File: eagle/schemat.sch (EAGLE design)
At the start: 30 parts, among them IC1 MEGA8-AI, Q1 N-MOSFET BSS138, Q2 N-MOSFET BSS138, U1 LCD-16X2SILK, Y1 16MHz

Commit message: Gotowa płytka
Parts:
- removed D1: GREEN, SparkFun-LED:LED-GREEN0603
- removed D2: RED, SparkFun-LED:LED-RED0603
- removed JP1, JP2, JP6, JP7: M02PTH, SparkFun-Connectors:M02PTH
- removed R3, R4: 100, SparkFun-Passives:RESISTOR0805-RES
- added PRZYCISKI_+-, PRZYCISKI_MIESZ_TEMP: (no value), SparkFun-Connectors:M03LOCK
- added TEMP_PRZEKAZNIK1, TEMP_PRZEKAZNIK2: M01PTH, SparkFun-Connectors:M01PTH
- added X2: MINI-USB-32005-301, con-cypressindustries:MINI-USB-32005-301
- L1: device inductors:MICC10 -> SparkFun-Passives:INDUCTOR0805
- renumbered JP10 to MIESZANIE_PRZEKAZNIK, JP3 to TEMP, JP4 to MIESZANIE, JP5 to ZAPISZ, JP8 to NAPIECIE, JP9 to TEMP_PRZEKAZNIK
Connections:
- removed net N$10: D2.C, R4.2
- removed net N$11: D1.A, IC1.PD0(RXD)
- removed net N$12: D1.C, R3.2
- removed net N$8: D2.A, IC1.PD1(TXD)
- new net MISO: IC1.PB4(MISO), X2.3
- new net MOSI: IC1.PB3(MOSI/OC2), X2.2
- new net SCK: IC1.PB5(SCK), X2.4
- net +5V: now also NAPIECIE.1, U$1.C, X2.1
- net DB4: now also IC1.PD7(AIN1); no longer IC1.PB2(SS/OC1B)
- net DB5: now also IC1.PB0(ICP); no longer IC1.PB3(MOSI/OC2)
- net DB6: now also IC1.PB1(OC1A); no longer IC1.PB4(MISO)
- net DB7: now also IC1.PB2(SS/OC1B); no longer IC1.PB5(SCK)
- net E: now also IC1.PD6(AIN0); no longer IC1.PB1(OC1A)
- net GND: now also PRZYCISKI_+-.3, PRZYCISKI_MIESZ_TEMP.3, X2.5; no longer JP1.2, JP2.2, JP6.2, JP7.2, R3.1, R4.1
- net MIESZANIE: now also IC1.PC5(ADC5/SCL); no longer IC1.PC4(ADC4/SDA)
- net PRZYCISK+: now also PRZYCISKI_+-.2; no longer JP6.1
- net PRZYCISK-: now also PRZYCISKI_+-.1; no longer JP7.1
- net PRZYCISK_MIESZANIE: now also IC1.PC4(ADC4/SDA), PRZYCISKI_MIESZ_TEMP.1; no longer IC1.PC2(ADC2), JP2.1
- net PRZYCISK_TEMP: now also IC1.PC3(ADC3), PRZYCISKI_MIESZ_TEMP.2; no longer IC1.PC1(ADC1), JP1.1
- net RS: now also IC1.PD5(T1); no longer IC1.PB0(ICP)
- net TEMP: now also IC1.PC2(ADC2); no longer IC1.PC3(ADC3)
- net VCC: no longer NAPIECIE.1, U$1.C
- net VDD: now also TEMP_PRZEKAZNIK1.1, TEMP_PRZEKAZNIK2.1
- net ZAPISZ: now also IC1.PC1(ADC1); no longer IC1.PC5(ADC5/SCL)

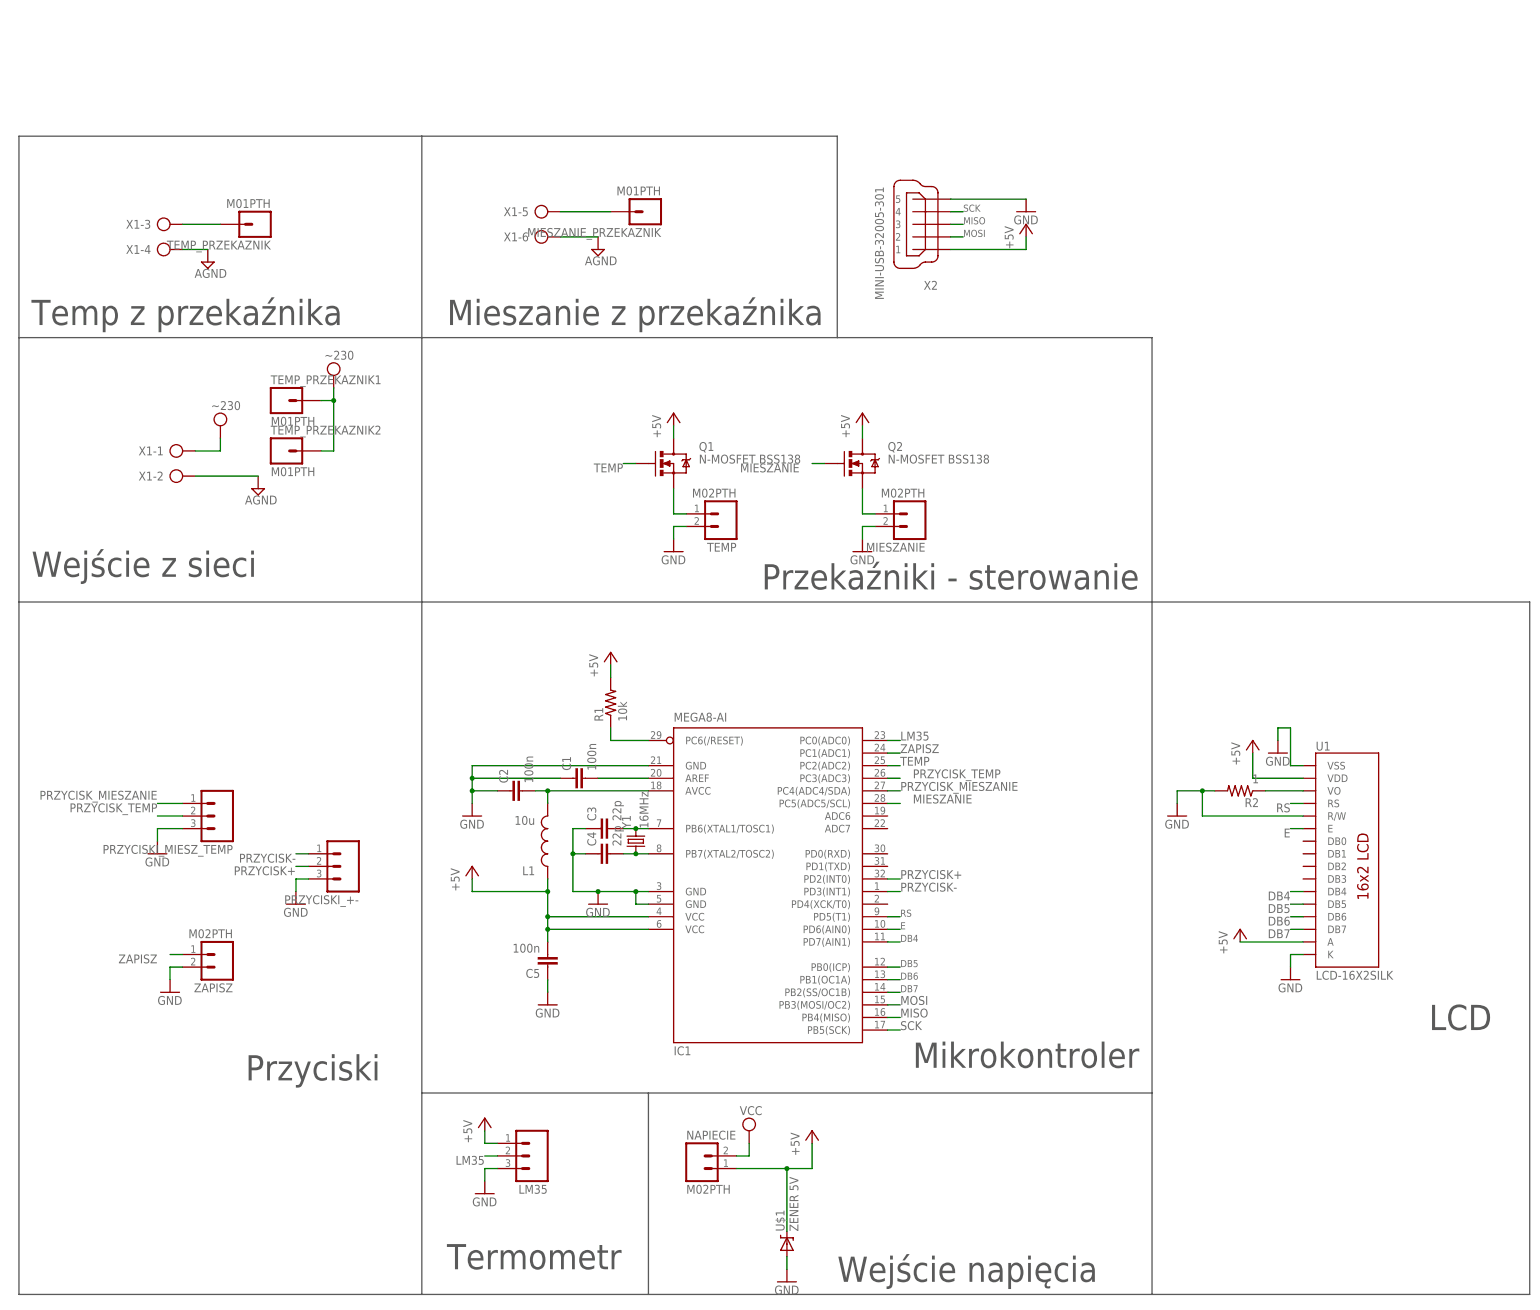
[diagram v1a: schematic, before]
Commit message: Poprawiony schemat
Nie dało się przylutować microUSB (zła biblioteka)
Nie podłączony RESET
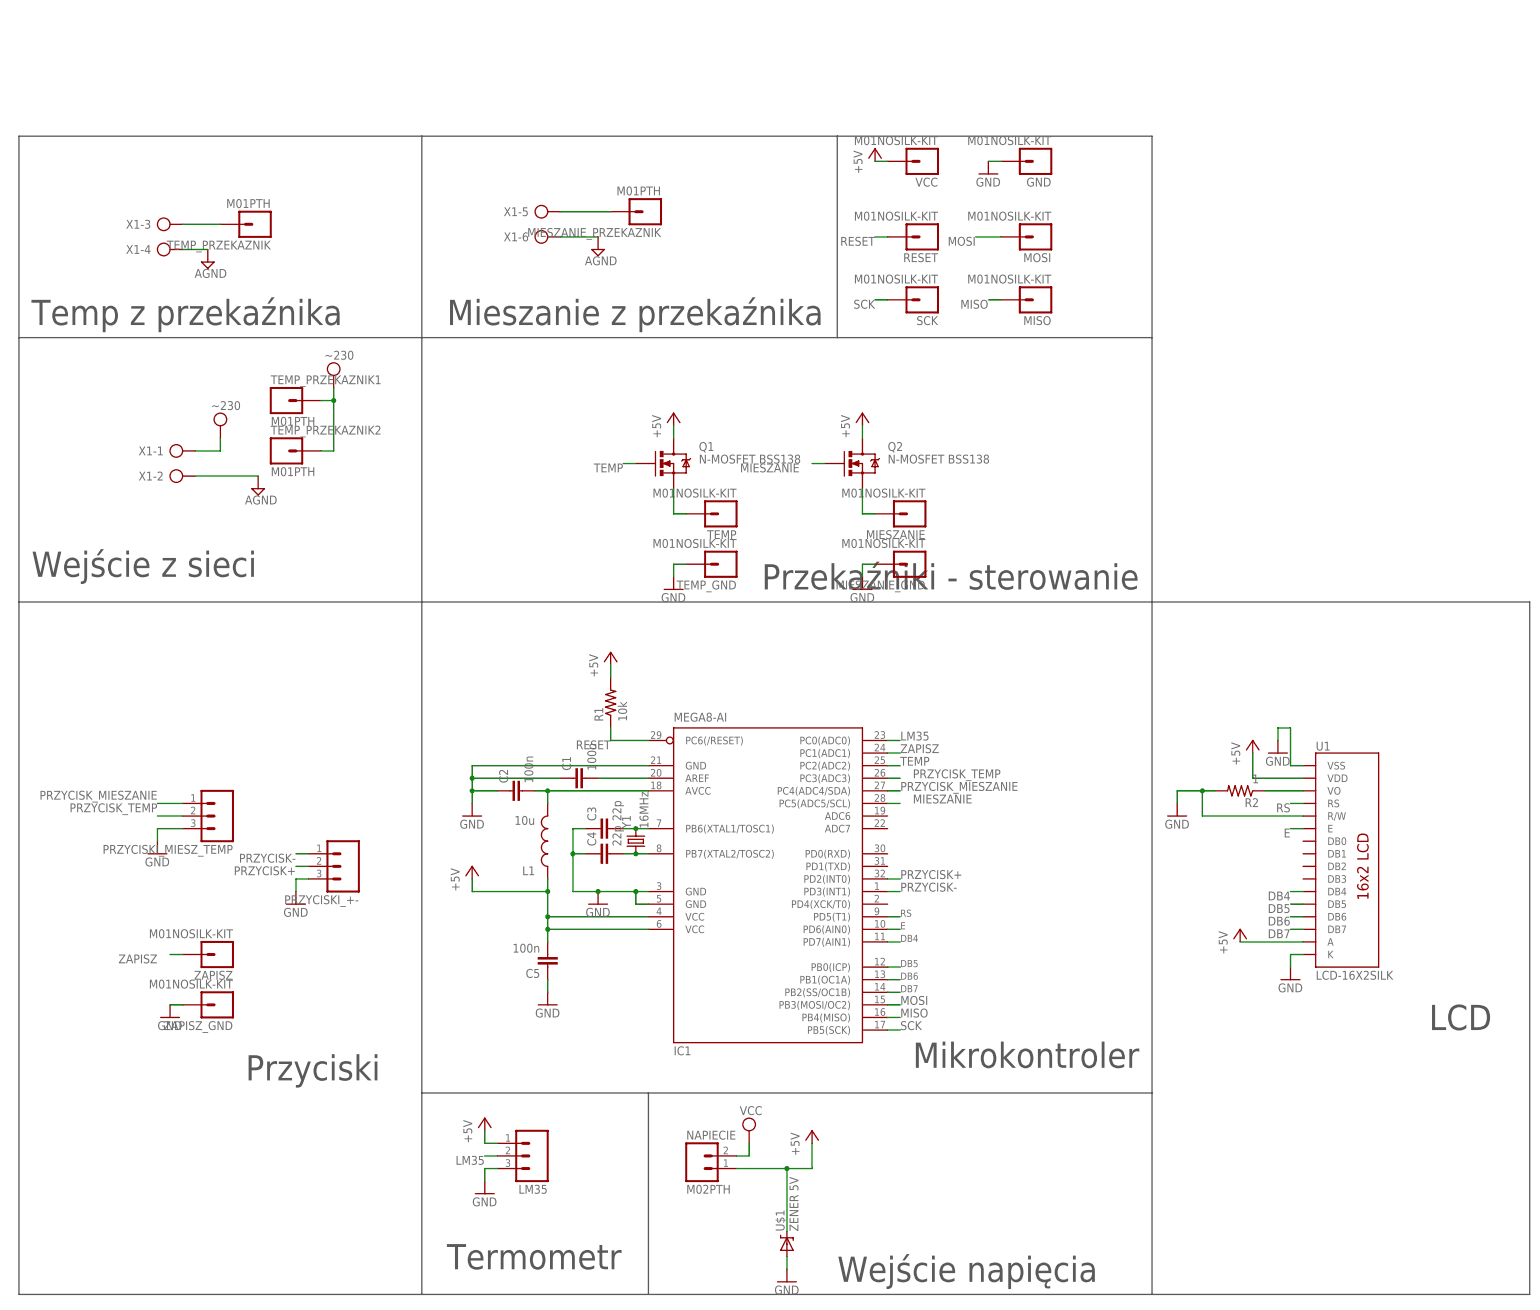
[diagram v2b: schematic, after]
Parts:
- removed X2: MINI-USB-32005-301, con-cypressindustries:MINI-USB-32005-301
- added GND, MIESZANIE_GND, MISO, MOSI, RESET, SCK, TEMP_GND, VCC, ZAPISZ_GND: M01NOSILK-KIT, SparkFun-Connectors:M01NOSILK-KIT
- MIESZANIE, TEMP, ZAPISZ: value M02PTH -> M01NOSILK-KIT; device SparkFun-Connectors:M02PTH -> SparkFun-Connectors:M01NOSILK-KIT
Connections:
- removed net N$1: IC1.PC6(/RESET), R1.1
- new net RESET: IC1.PC6(/RESET), R1.1, RESET.1
- net +5V: now also VCC.1; no longer X2.1
- net GND: now also GND.1, MIESZANIE_GND.1, TEMP_GND.1, ZAPISZ_GND.1; no longer MIESZANIE.2, TEMP.2, X2.5, ZAPISZ.2
- net MISO: now also MISO.1; no longer X2.3
- net MOSI: now also MOSI.1; no longer X2.2
- net SCK: now also SCK.1; no longer X2.4
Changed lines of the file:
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@@
 <part name="P+4" library="supply1" deviceset="+5V" device=""/>
 <part name="P+5" library="supply1" deviceset="+5V" device=""/>
-<part name="TEMP" library="SparkFun-Connectors" deviceset="M02" device="PTH"/>
-<part name="MIESZANIE" library="SparkFun-Connectors" deviceset="M02" device="PTH"/>
-<part name="GND7" library="SparkFun-Aesthetics" deviceset="GND" device=""/>
-<part name="GND8" library="SparkFun-Aesthetics" deviceset="GND" device=""/>
-<part name="ZAPISZ" library="SparkFun-Connectors" deviceset="M02" device="PTH"/>
-<part name="GND9" library="SparkFun-Aesthetics" deviceset="GND" device=""/>
+<part name="TEMP" library="SparkFun-Connectors" deviceset="M01" device="NOSILK-KIT"/>
+<part name="MIESZANIE" library="SparkFun-Connectors" deviceset="M01" device="NOSILK-KIT"/>
+<part name="ZAPISZ" library="SparkFun-Connectors" deviceset="M01" device="NOSILK-KIT" value="M01NOSILK-KIT"/>
 <part name="U1" library="SparkFun-Displays" deviceset="LCD-16X2" device="SILK"/>
 <part name="GND10" library="SparkFun-Aesthetics" deviceset="GND" device=""/>
@@
 <part name="TEMP_PRZEKAZNIK2" library="SparkFun-Connectors" deviceset="M01" device="PTH"/>
 <part name="SUPPLY6" library="supply2" deviceset="VDD" device="" value="~230"/>
-<part name="X2" library="con-cypressindustries" deviceset="MINI-USB-" device="32005-301"/>
+<part name="ZAPISZ_GND" library="SparkFun-Connectors" deviceset="M01" device="NOSILK-KIT"/>
+<part name="GND9" library="SparkFun-Aesthetics" deviceset="GND" device=""/>
+<part name="VCC" library="SparkFun-Connectors" deviceset="M01" device="NOSILK-KIT"/>
+<part name="GND" library="SparkFun-Connectors" deviceset="M01" device="NOSILK-KIT"/>
+<part name="RESET" library="SparkFun-Connectors" deviceset="M01" device="NOSILK-KIT"/>
+<part name="MOSI" library="SparkFun-Connectors" deviceset="M01" device="NOSILK-KIT"/>
+<part name="SCK" library="SparkFun-Connectors" deviceset="M01" device="NOSILK-KIT"/>
+<part name="MISO" library="SparkFun-Connectors" deviceset="M01" device="NOSILK-KIT"/>
 <part name="P+9" library="supply1" deviceset="+5V" device=""/>
 <part name="GND6" library="SparkFun-Aesthetics" deviceset="GND" device=""/>
+<part name="TEMP_GND" library="SparkFun-Connectors" deviceset="M01" device="NOSILK-KIT"/>
+<part name="MIESZANIE_GND" library="SparkFun-Connectors" deviceset="M01" device="NOSILK-KIT"/>
+<part name="GND7" library="SparkFun-Aesthetics" deviceset="GND" device=""/>
+<part name="GND8" library="SparkFun-Aesthetics" deviceset="GND" device=""/>
 </parts>
 <sheets>
@@
 <wire x1="63.5" y1="208.28" x2="63.5" y2="167.64" width="0.1524" layer="97"/>
 <text x="-15.24" y="170.18" size="5.08" layer="97">Mieszanie z przekaźnika</text>
+<wire x1="127" y1="167.64" x2="127" y2="208.28" width="0.1524" layer="97"/>
+<wire x1="127" y1="208.28" x2="63.5" y2="208.28" width="0.1524" layer="97"/>
 </plain>
 <instances>
@@
 <instance part="TEMP" gate="G$1" x="40.64" y="132.08" rot="R180"/>
 <instance part="MIESZANIE" gate="G$1" x="78.74" y="132.08" rot="R180"/>
-<instance part="GND7" gate="1" x="30.48" y="124.46"/>
-<instance part="GND8" gate="1" x="68.58" y="124.46"/>
 <instance part="ZAPISZ" gate="G$1" x="-60.96" y="43.18" rot="R180"/>
-<instance part="GND9" gate="1" x="-71.12" y="35.56"/>
 <instance part="U1" gate="G$1" x="167.64" y="60.96"/>
 <instance part="GND10" gate="1" x="154.94" y="38.1"/>
@@
 <instance part="TEMP_PRZEKAZNIK2" gate="G$1" x="-48.26" y="144.78"/>
 <instance part="SUPPLY6" gate="G$1" x="-38.1" y="160.02"/>
-<instance part="X2" gate="G$1" x="81.28" y="190.5" rot="R180"/>
-<instance part="P+9" gate="1" x="101.6" y="190.5"/>
-<instance part="GND6" gate="1" x="101.6" y="193.04"/>
+<instance part="ZAPISZ_GND" gate="G$1" x="-60.96" y="33.02" rot="R180"/>
+<instance part="GND9" gate="1" x="-71.12" y="30.48"/>
+<instance part="VCC" gate="G$1" x="81.28" y="203.2" rot="R180"/>
+<instance part="GND" gate="G$1" x="104.14" y="203.2" rot="R180"/>
+<instance part="RESET" gate="G$1" x="81.28" y="187.96" rot="R180"/>
+<instance part="MOSI" gate="G$1" x="104.14" y="187.96" rot="R180"/>
+<instance part="SCK" gate="G$1" x="81.28" y="175.26" rot="R180"/>
+<instance part="MISO" gate="G$1" x="104.14" y="175.26" rot="R180"/>
+<instance part="P+9" gate="1" x="71.12" y="205.74"/>
+<instance part="GND6" gate="1" x="93.98" y="200.66"/>
+<instance part="TEMP_GND" gate="G$1" x="40.64" y="121.92" rot="R180"/>
+<instance part="MIESZANIE_GND" gate="G$1" x="78.74" y="121.92" rot="R180"/>
+<instance part="GND7" gate="1" x="30.48" y="116.84"/>
+<instance part="GND8" gate="1" x="68.58" y="116.84"/>
 </instances>
 <busses>
@@
 </segment>
 <segment>
-<pinref part="X2" gate="G$1" pin="1"/>
-<wire x1="86.36" y1="185.42" x2="101.6" y2="185.42" width="0.1524" layer="91"/>
-<wire x1="101.6" y1="185.42" x2="101.6" y2="187.96" width="0.1524" layer="91"/>
+<pinref part="VCC" gate="G$1" pin="1"/>
+<wire x1="73.66" y1="203.2" x2="71.12" y2="203.2" width="0.1524" layer="91"/>
 <pinref part="P+9" gate="1" pin="+5V"/>
 </segment>
 </net>
-<net name="N$1" class="0">
+<net name="RESET" class="0">
 <segment>
 <pinref part="R1" gate="G$1" pin="1"/>
@@
 <pinref part="IC1" gate="G$1" pin="PC6(/RESET)"/>
 <wire x1="17.78" y1="86.36" x2="25.4" y2="86.36" width="0.1524" layer="91"/>
+<label x="17.78" y="86.36" size="1.778" layer="95" rot="R180"/>
+</segment>
+<segment>
+<pinref part="RESET" gate="G$1" pin="1"/>
+<wire x1="73.66" y1="187.96" x2="71.12" y2="187.96" width="0.1524" layer="91"/>
+<label x="71.12" y="187.96" size="1.778" layer="95" rot="R180"/>
 </segment>
 </net>
@@
 </segment>
 <segment>
-<pinref part="MIESZANIE" gate="G$1" pin="2"/>
-<pinref part="GND8" gate="1" pin="GND"/>
-<wire x1="71.12" y1="129.54" x2="68.58" y2="129.54" width="0.1524" layer="91"/>
-<wire x1="68.58" y1="129.54" x2="68.58" y2="127" width="0.1524" layer="91"/>
-</segment>
-<segment>
-<pinref part="TEMP" gate="G$1" pin="2"/>
-<pinref part="GND7" gate="1" pin="GND"/>
-<wire x1="33.02" y1="129.54" x2="30.48" y2="129.54" width="0.1524" layer="91"/>
-<wire x1="30.48" y1="129.54" x2="30.48" y2="127" width="0.1524" layer="91"/>
-</segment>
-<segment>
-<pinref part="ZAPISZ" gate="G$1" pin="2"/>
-<pinref part="GND9" gate="1" pin="GND"/>
-<wire x1="-68.58" y1="40.64" x2="-71.12" y2="40.64" width="0.1524" layer="91"/>
-<wire x1="-71.12" y1="40.64" x2="-71.12" y2="38.1" width="0.1524" layer="91"/>
-</segment>
-<segment>
 <pinref part="U1" gate="G$1" pin="K"/>
 <pinref part="GND10" gate="1" pin="GND"/>
@@
 </segment>
 <segment>
-<pinref part="X2" gate="G$1" pin="5"/>
-<wire x1="86.36" y1="195.58" x2="101.6" y2="195.58" width="0.1524" layer="91"/>
+<pinref part="ZAPISZ_GND" gate="G$1" pin="1"/>
+<wire x1="-68.58" y1="33.02" x2="-71.12" y2="33.02" width="0.1524" layer="91"/>
+<pinref part="GND9" gate="1" pin="GND"/>
+</segment>
+<segment>
+<pinref part="GND" gate="G$1" pin="1"/>
+<wire x1="96.52" y1="203.2" x2="93.98" y2="203.2" width="0.1524" layer="91"/>
 <pinref part="GND6" gate="1" pin="GND"/>
+</segment>
+<segment>
+<pinref part="GND7" gate="1" pin="GND"/>
+<wire x1="30.48" y1="119.38" x2="30.48" y2="121.92" width="0.1524" layer="91"/>
+<pinref part="TEMP_GND" gate="G$1" pin="1"/>
+<wire x1="30.48" y1="121.92" x2="33.02" y2="121.92" width="0.1524" layer="91"/>
+</segment>
+<segment>
+<pinref part="GND8" gate="1" pin="GND"/>
+<wire x1="68.58" y1="119.38" x2="68.58" y2="121.92" width="0.1524" layer="91"/>
+<pinref part="MIESZANIE_GND" gate="G$1" pin="1"/>
+<wire x1="68.58" y1="121.92" x2="71.12" y2="121.92" width="0.1524" layer="91"/>
 </segment>
 </net>
@@
 </segment>
 <segment>
-<pinref part="X2" gate="G$1" pin="2"/>
-<wire x1="86.36" y1="187.96" x2="88.9" y2="187.96" width="0.1524" layer="91"/>
-<label x="88.9" y="187.96" size="1.4224" layer="95"/>
+<pinref part="MOSI" gate="G$1" pin="1"/>
+<wire x1="96.52" y1="187.96" x2="91.44" y2="187.96" width="0.1524" layer="91"/>
+<label x="91.44" y="187.96" size="1.778" layer="95" rot="R180"/>
 </segment>
 </net>
@@
 </segment>
 <segment>
-<pinref part="X2" gate="G$1" pin="3"/>
-<wire x1="86.36" y1="190.5" x2="88.9" y2="190.5" width="0.1524" layer="91"/>
-<label x="88.9" y="190.5" size="1.4224" layer="95"/>
+<pinref part="MISO" gate="G$1" pin="1"/>
+<wire x1="96.52" y1="175.26" x2="93.98" y2="175.26" width="0.1524" layer="91"/>
+<label x="93.98" y="175.26" size="1.778" layer="95" rot="R180"/>
 </segment>
 </net>
@@
 </segment>
 <segment>
-<pinref part="X2" gate="G$1" pin="4"/>
-<wire x1="86.36" y1="193.04" x2="88.9" y2="193.04" width="0.1524" layer="91"/>
-<label x="88.9" y="193.04" size="1.4224" layer="95"/>
+<pinref part="SCK" gate="G$1" pin="1"/>
+<wire x1="73.66" y1="175.26" x2="71.12" y2="175.26" width="0.1524" layer="91"/>
+<label x="71.12" y="175.26" size="1.778" layer="95" rot="R180"/>
 </segment>
 </net>
@@
 </sheet>
 </sheets>
+<errors>
+</errors>
 </schematic>
 </drawing>
